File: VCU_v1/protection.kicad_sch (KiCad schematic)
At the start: 3 parts, among them Q1 PMOS

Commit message: left to do before layout: wire DRS/Debug LEDs to connector, add BRUHbus ports
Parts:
- added D7: SMBJ30CA, symbol Device:D_TVS
- D2: value 12Vz -> 27Vz; LCSC P/N C669032 -> C712317; Mouser P/N 833-SMAF4742A-TP -> 833-SMAF4750A-TP; P/N SMAF4742A-TP -> SMAF4750A-TP
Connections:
- net GND: now also D7.1 (A1)
- net VBAT_FILT: now also D7.2 (A2)
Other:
- note added: "Reverse Polarity Protection + TVS"
- note removed: "Reverse Polarity Protection"
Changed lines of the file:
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@@
 	(rectangle
 		(start 68.58 41.91)
-		(end 129.54 87.63)
+		(end 171.45 87.63)
 		(stroke
 			(width 0)
@@
 		)
 	)
-	(text "Reverse Polarity Protection\n"
+	(text "Reverse Polarity Protection + TVS\n\n"
 		(exclude_from_sim no)
 		(at 97.536 38.862 0)
@@
 	)
 	(junction
+		(at 127 57.15)
+		(diameter 0)
+		(color 0 0 0 0)
+	)
+	(junction
 		(at 106.68 57.15)
 		(diameter 0)
@@
 	(wire
 		(pts
+			(xy 127 57.15) (xy 152.4 57.15)
+		)
+		(stroke
+			(width 0)
+			(type default)
+		)
+	)
+	(wire
+		(pts
 			(xy 78.74 57.15) (xy 90.17 57.15)
 		)
@@
 	(wire
 		(pts
-			(xy 106.68 57.15) (xy 114.3 57.15)
+			(xy 106.68 57.15) (xy 127 57.15)
 		)
 		(stroke
@@
 	(wire
 		(pts
+			(xy 127 62.23) (xy 127 57.15)
+		)
+		(stroke
+			(width 0)
+			(type default)
+		)
+	)
+	(wire
+		(pts
 			(xy 95.25 73.66) (xy 95.25 76.2)
+		)
+		(stroke
+			(width 0)
+			(type default)
+		)
+	)
+	(wire
+		(pts
+			(xy 127 69.85) (xy 127 76.2)
 		)
 		(stroke
@@
 	(hierarchical_label "VBAT_FILT"
 		(shape input)
-		(at 114.3 57.15 0)
+		(at 152.4 57.15 0)
 		(effects
 			(font
@@
 			)
 		)
-		(property "Value" "12Vz"
+		(property "Value" "27Vz"
 			(at 109.22 62.2299 90)
 			(effects
@@
 			)
 		)
-		(property "P/N" "SMAF4742A-TP "
+		(property "P/N" "SMAF4750A-TP "
 			(at 106.68 60.96 90)
 			(effects
@@
 			)
 		)
-		(property "Mouser P/N" "833-SMAF4742A-TP"
+		(property "Mouser P/N" "833-SMAF4750A-TP "
 			(at 106.68 60.96 90)
 			(effects
@@
 			)
 		)
-		(property "LCSC P/N" "C669032"
+		(property "LCSC P/N" "C712317"
 			(at 106.68 60.96 90)
 			(effects
@@
 				(path "/4ee6c2ad-9a1b-4276-b3cf-1cc8dc52967e/9e4b5f8d-93dc-46d5-aa92-d0e0d2e07b3d/b7d8a0a7-c635-4617-919c-9464d63ae6b1"
 					(reference "D2")
+					(unit 1)
+				)
+			)
+		)
+	)
+	(symbol
+		(lib_id "power:GND")
+		(at 127 76.2 0)
+		(unit 1)
+		(exclude_from_sim no)
+		(in_bom yes)
+		(on_board yes)
+		(dnp no)
+		(fields_autoplaced yes)
+		(property "Reference" "#PWR0102"
+			(at 127 82.55 0)
+			(effects
+				(font
+					(size 1.27 1.27)
+				)
+				(hide yes)
+			)
+		)
+		(property "Value" "GND"
+			(at 127 81.28 0)
+			(effects
+				(font
+					(size 1.27 1.27)
+				)
+			)
+		)
+		(property "Footprint" ""
+			(at 127 76.2 0)
+			(effects
+				(font
+					(size 1.27 1.27)
+				)
+				(hide yes)
+			)
+		)
+		(property "Datasheet" ""
+			(at 127 76.2 0)
+			(effects
+				(font
+					(size 1.27 1.27)
+				)
+				(hide yes)
+			)
+		)
+		(property "Description" "Power symbol creates a global label with name \"GND\" , ground"
+			(at 127 76.2 0)
+			(effects
+				(font
+					(size 1.27 1.27)
+				)
+				(hide yes)
+			)
+		)
+		(pin "1"
+		)
+		(instances
+			(project "VCU_v1"
+				(path "/4ee6c2ad-9a1b-4276-b3cf-1cc8dc52967e/9e4b5f8d-93dc-46d5-aa92-d0e0d2e07b3d/b7d8a0a7-c635-4617-919c-9464d63ae6b1"
+					(reference "#PWR0102")
 					(unit 1)
 				)
@@
 					(unit 1)
 				)
+			)
+		)
+	)
+	(symbol
+		(lib_id "Device:D_TVS")
+		(at 127 66.04 90)
+		(unit 1)
+		(exclude_from_sim no)
+		(in_bom yes)
+		(on_board yes)
+		(dnp no)
+		(fields_autoplaced yes)
+		(property "Reference" "D7"
+			(at 129.54 64.7699 90)
+			(effects
+				(font
+					(size 1.27 1.27)
+				)
+				(justify right)
+			)
+		)
+		(property "Value" "SMBJ30CA"
+			(at 129.54 67.3099 90)
+			(effects
+				(font
+					(size 1.27 1.27)
+				)
+				(justify right)
+			)
+		)
+		(property "Footprint" ""
+			(at 127 66.04 0)
+			(effects
+				(font
+					(size 1.27 1.27)
+				)
+				(hide yes)
+			)
+		)
+		(property "Datasheet" "https://www.littelfuse.com/page-not-found?url=/assetdocs/tvs-diodes-smbj-series-datasheet?assetguid=09A6AE9A-73CB-4AC4-ACAC-E6DAB92AB953"
+			(at 127 66.04 0)
+			(effects
+				(font
+					(size 1.27 1.27)
+				)
+				(hide yes)
+			)
+		)
+		(property "Description" "Bidirectional transient-voltage-suppression diode"
+			(at 127 66.04 0)
+			(effects
+				(font
+					(size 1.27 1.27)
+				)
+				(hide yes)
+			)
+		)
+		(property "P/N" "SMBJ30CA"
+			(at 127 66.04 90)
+			(effects
+				(font
+					(size 1.27 1.27)
+				)
+				(hide yes)
+			)
+		)
+		(property "Mouser P/N" "576-SMBJ30CA "
+			(at 127 66.04 90)
+			(effects
+				(font
+					(size 1.27 1.27)
+				)
+				(hide yes)
+			)
+		)
+		(property "LCSC P/N" "C8837"
+			(at 127 66.04 90)
+			(effects
+				(font
+					(size 1.27 1.27)
+				)
+				(hide yes)
+			)
+		)
+		(pin "1"
+		)
+		(pin "2"
+		)
+		(instances
+			(project ""
+				(path "/4ee6c2ad-9a1b-4276-b3cf-1cc8dc52967e/9e4b5f8d-93dc-46d5-aa92-d0e0d2e07b3d/b7d8a0a7-c635-4617-919c-9464d63ae6b1"
+					(reference "D7")
+					(unit 1)
+				)

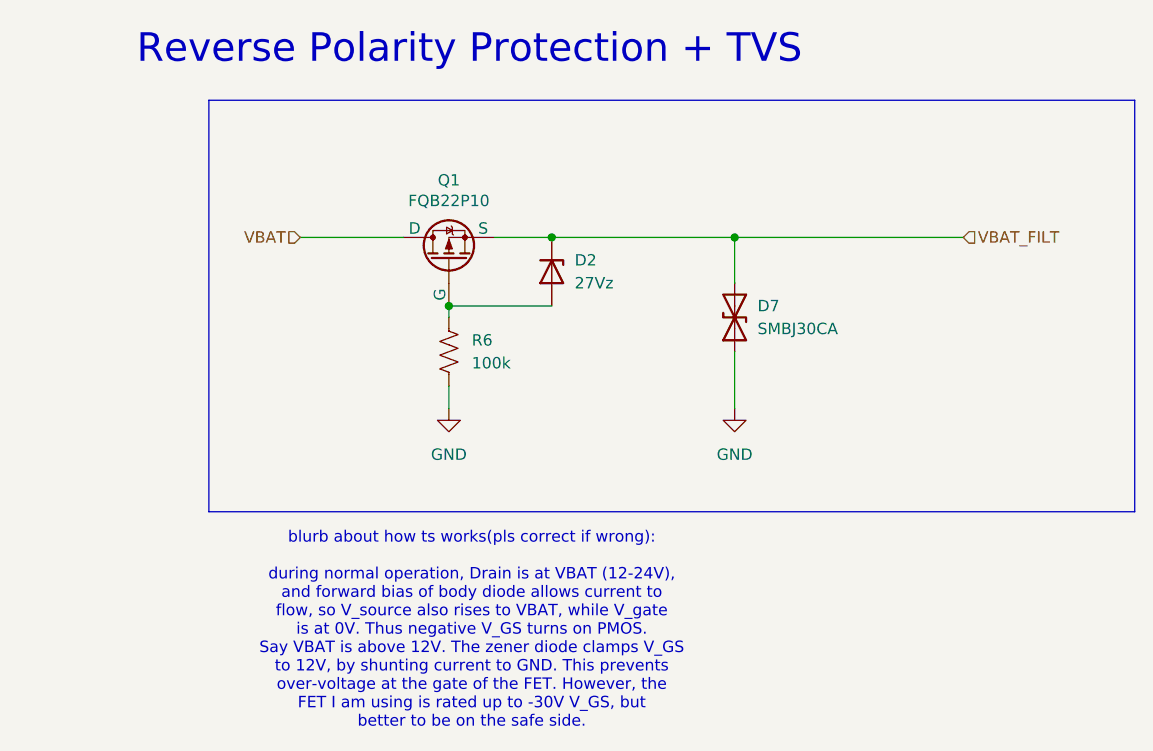
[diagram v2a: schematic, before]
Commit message: v1 schematic (actually) complete, let the layout commence
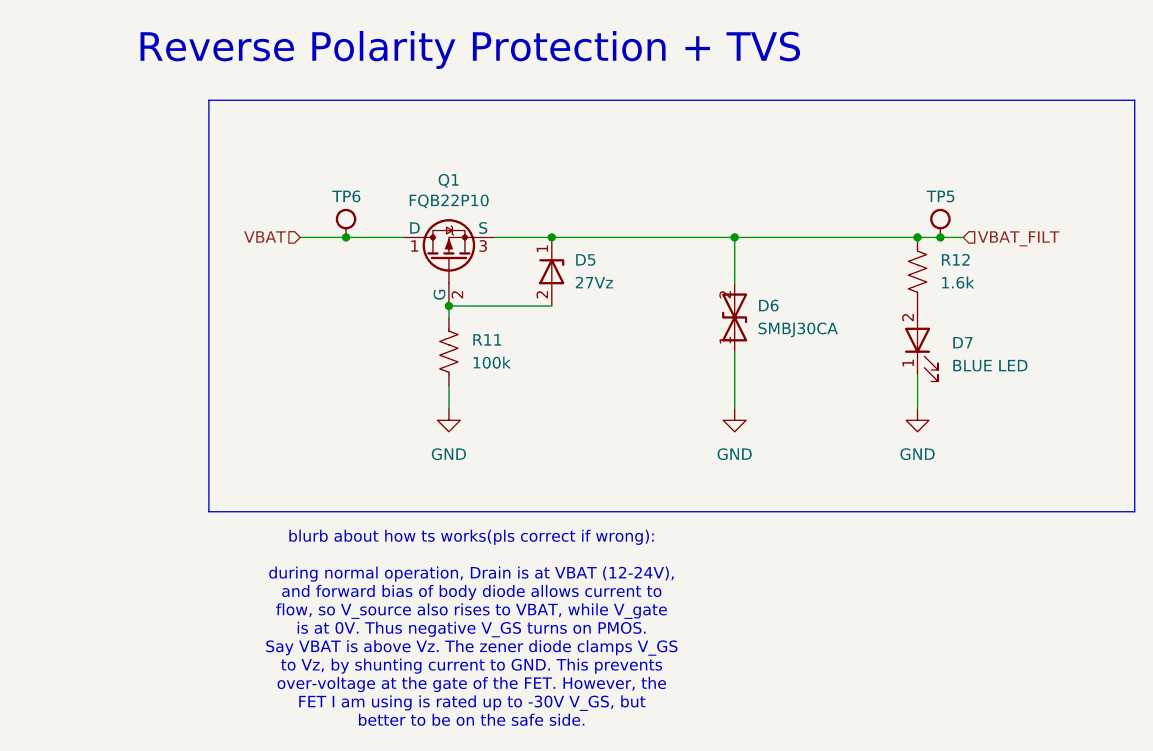
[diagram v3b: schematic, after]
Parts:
- added D7: BLUE LED, LED_SMD:LED_0201_0603Metric_Pad0.64x0.40mm_HandSolder, symbol Device:LED
- added R12: 1.6k, Resistor_SMD:R_0603_1608Metric_Pad0.98x0.95mm_HandSolder, symbol BFR Resistors:RMCF0603FT1K60
- added TP5, TP6: RH-5015, TestPoint:TestPoint_Keystone_5015_Micro_Mini, symbol .Test-Point:RH-5015
- D5: renamed from D2; footprint (none) -> Diode_SMD:D_SMA
- D6: renamed from D7; footprint (none) -> Diode_SMD:D_SMB
- Q1: footprint (none) -> FQB22P10:Untitled
- renumbered R6 to R11
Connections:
- net GND: now also D7.1 (K)
- net VBAT: now also TP6.1
- net VBAT_FILT: now also R12.2, TP5.1
- new net: D7.2 (A), R12.1
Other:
- note added: "blurb about how ts works(pls correct if wrong): during normal operation, Drain is at VBAT (12-24V), and forward bias of body diode allows current to flow, so V_source also rises to VBAT, while V_gate is at 0V. Thus negative V_GS turns on PMOS. Say VBAT is above Vz. The zener diode clamps V_GS to Vz, by shunting current to GND. This prevents over-voltage at the gate of the FET. However, the FET I 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"
- note removed: "blurb about how ts works(pls correct if wrong): during normal operation, Drain is at VBAT (12-24V), and forward bias of body diode allows current to flow, so V_source also rises to VBAT, while V_gate is at 0V. Thus negative V_GS turns on PMOS. Say VBAT is above 12V. The zener diode clamps V_GS to 12V, by shunting current to GND. This prevents over-voltage at the gate of the FET. However, the FET 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"

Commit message: vcu placements complete
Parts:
- D7: footprint LED_SMD:LED_0201_0603Metric_Pad0.64x0.40mm_HandSolder -> LED_SMD:LED_0603_1608Metric_Pad1.05x0.95mm_HandSolder
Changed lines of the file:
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@@
 			)
 		)
-		(property "Footprint" "LED_SMD:LED_0201_0603Metric_Pad0.64x0.40mm_HandSolder"
+		(property "Footprint" "LED_SMD:LED_0603_1608Metric_Pad1.05x0.95mm_HandSolder"
 			(at 147.32 68.58 0)
 			(effects

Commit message: almost done i promise
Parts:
- removed R12: 1.6k, Resistor_SMD:R_0603_1608Metric_Pad0.98x0.95mm_HandSolder, symbol BFR Resistors:RMCF0603FT1K60
- added R3: 2.4k, Resistor_SMD:R_0603_1608Metric_Pad0.98x0.95mm_HandSolder, symbol BFR Resistors:RMCF0603FT2K40
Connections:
- net VBAT_FILT: now also R3.2
- net at D7.2 (A): now also R3.1
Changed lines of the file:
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@@
+	)
+	(junction
+		(at 147.32 57.15)
+		(diameter 0)
+		(color 0 0 0 0)
 	)
 	(junction
@@
 	)
 	(junction
-		(at 147.32 57.15)
-		(diameter 0)
-		(color 0 0 0 0)
-	)
-	(junction
 		(at 83.82 57.15)
 		(diameter 0)
@@
 	(wire
 		(pts
-			(xy 147.32 57.15) (xy 149.86 57.15)
+			(xy 83.82 57.15) (xy 90.17 57.15)
 		)
 		(stroke
@@
 	(wire
 		(pts
-			(xy 83.82 57.15) (xy 90.17 57.15)
+			(xy 78.74 57.15) (xy 83.82 57.15)
 		)
 		(stroke
@@
 	(wire
 		(pts
-			(xy 78.74 57.15) (xy 83.82 57.15)
+			(xy 106.68 57.15) (xy 127 57.15)
 		)
 		(stroke
@@
 	(wire
 		(pts
-			(xy 106.68 57.15) (xy 127 57.15)
+			(xy 95.25 64.77) (xy 106.68 64.77)
 		)
 		(stroke
@@
 	(wire
 		(pts
-			(xy 95.25 64.77) (xy 106.68 64.77)
+			(xy 100.33 57.15) (xy 106.68 57.15)
 		)
 		(stroke
@@
 	(wire
 		(pts
-			(xy 100.33 57.15) (xy 106.68 57.15)
+			(xy 147.32 57.15) (xy 149.86 57.15)
 		)
 		(stroke
@@
 				(path "/4ee6c2ad-9a1b-4276-b3cf-1cc8dc52967e/9e4b5f8d-93dc-46d5-aa92-d0e0d2e07b3d/b7d8a0a7-c635-4617-919c-9464d63ae6b1"
 					(reference "Q1")
-					(unit 1)
-				)
-			)
-		)
-	)
-	(symbol
-		(lib_id "BFR Resistors:RMCF0603FT1K60")
-		(at 147.32 60.96 90)
-		(unit 1)
-		(exclude_from_sim no)
-		(in_bom yes)
-		(on_board yes)
-		(dnp no)
-		(fields_autoplaced yes)
-		(property "Reference" "R12"
-			(at 149.86 59.6899 90)
-			(effects
-				(font
-					(size 1.27 1.27)
-				)
-				(justify right)
-			)
-		)
-		(property "Value" "1.6k"
-			(at 149.86 62.2299 90)
-			(effects
-				(font
-					(size 1.27 1.27)
-				)
-				(justify right)
-			)
-		)
-		(property "Footprint" "Resistor_SMD:R_0603_1608Metric_Pad0.98x0.95mm_HandSolder"
-			(at 149.86 60.96 0)
-			(effects
-				(font
-					(size 1.27 1.27)
-				)
-				(hide yes)
-			)
-		)
-		(property "Datasheet" "https://www.seielect.com/catalog/sei-rmcf_rmcp.pdf"
-			(at 151.13 60.96 0)
-			(effects
-				(font
-					(size 1.27 1.27)
-				)
-				(hide yes)
-			)
-		)
-		(property "Description" "1.6kΩ 0603 Resistor"
-			(at 147.32 60.96 0)
-			(effects
-				(font
-					(size 1.27 1.27)
-				)
-				(hide yes)
-			)
-		)
-		(property "Sim.Device" "SUBCKT"
-			(at 152.4 60.96 0)
-			(effects
-				(font
-					(size 1.27 1.27)
-				)
-				(hide yes)
-			)
-		)
-		(property "Sim.Pins" "1=P1 2=P2"
-			(at 153.67 60.96 0)
-			(effects
-				(font
-					(size 1.27 1.27)
-				)
-				(hide yes)
-			)
-		)
-		(property "Sim.Library" "${BFRUH_DIR}/Electronics/spice_models/bfr_resistors/RMCF0603FT1K60.lib"
-			(at 154.94 60.96 0)
-			(effects
-				(font
-					(size 1.27 1.27)
-				)
-				(hide yes)
-			)
-		)
-		(property "Sim.Name" "RMCF0603FT1K60"
-			(at 156.21 60.96 0)
-			(effects
-				(font
-					(size 1.27 1.27)
-				)
-				(hide yes)
-			)
-		)
-		(property "Pretty Name" "1.6kΩ 0603 Resistor"
-			(at 157.48 60.96 0)
-			(effects
-				(font
-					(size 1.27 1.27)
-				)
-				(hide yes)
-			)
-		)
-		(property "Qty/Unit" ""
-			(at 158.75 60.96 0)
-			(effects
-				(font
-					(size 1.27 1.27)
-				)
-				(hide yes)
-			)
-		)
-		(property "Cost/Unit" ""
-			(at 160.02 60.96 0)
-			(effects
-				(font
-					(size 1.27 1.27)
-				)
-				(hide yes)
-			)
-		)
-		(property "Order From" "Mouser"
-			(at 161.29 60.96 0)
-			(effects
-				(font
-					(size 1.27 1.27)
-				)
-				(hide yes)
-			)
-		)
-		(property "Digikey P/N" "RMCF0603FT1K60CT-ND"
-			(at 162.56 60.96 0)
-			(effects
-				(font
-					(size 1.27 1.27)
-				)
-				(hide yes)
-			)
-		)
-		(property "Mouser P/N" "708-RMCF0603FT1K60"
-			(at 162.56 60.96 0)
-			(effects
-				(font
-					(size 1.27 1.27)
-				)
-				(hide yes)
-			)
-		)
-		(property "LCSC P/N" "C22847"
-			(at 162.56 60.96 0)
-			(effects
-				(font
-					(size 1.27 1.27)
-				)
-				(hide yes)
-			)
-		)
-		(property "JLCPCB Basic Part" "No"
-			(at 162.56 60.96 0)
-			(effects
-				(font
-					(size 1.27 1.27)
-				)
-				(hide yes)
-			)
-		)
-		(property "Created by" "resistor_generator.py script using e24_resistor_bible_spec.txt"
-			(at 162.56 60.96 0)
-			(effects
-				(font
-					(size 1.27 1.27)
-				)
-				(hide yes)
-			)
-		)
-		(pin "2"
-		)
-		(pin "1"
-		)
-		(instances
-			(project "VCU_v1"
-				(path "/4ee6c2ad-9a1b-4276-b3cf-1cc8dc52967e/9e4b5f8d-93dc-46d5-aa92-d0e0d2e07b3d/b7d8a0a7-c635-4617-919c-9464d63ae6b1"
-					(reference "R12")
 					(unit 1)
 				)
@@
 					(unit 1)
 				)
+			)
+		)
+	)
+	(symbol
+		(lib_id "BFR Resistors:RMCF0603FT2K40")
+		(at 147.32 60.96 90)
+		(unit 1)
+		(exclude_from_sim no)
+		(in_bom yes)
+		(on_board yes)
+		(dnp no)
+		(fields_autoplaced yes)
+		(property "Reference" "R3"
+			(at 149.86 59.6899 90)
+			(effects
+				(font
+					(size 1.27 1.27)
+				)
+				(justify right)
+			)
+		)
+		(property "Value" "2.4k"
+			(at 149.86 62.2299 90)
+			(effects
+				(font
+					(size 1.27 1.27)
+				)
+				(justify right)
+			)
+		)
+		(property "Footprint" "Resistor_SMD:R_0603_1608Metric_Pad0.98x0.95mm_HandSolder"
+			(at 149.86 60.96 0)
+			(effects
+				(font
+					(size 1.27 1.27)
+				)
+				(hide yes)
+			)
+		)
+		(property "Datasheet" "https://www.seielect.com/catalog/sei-rmcf_rmcp.pdf"
+			(at 151.13 60.96 0)
+			(effects
+				(font
+					(size 1.27 1.27)
+				)
+				(hide yes)
+			)
+		)
+		(property "Description" "2.4kΩ 0603 JLCPCB Basic Resistor"
+			(at 147.32 60.96 0)
+			(effects
+				(font
+					(size 1.27 1.27)
+				)
+				(hide yes)
+			)
+		)
+		(property "Sim.Device" "SUBCKT"
+			(at 152.4 60.96 0)
+			(effects
+				(font
+					(size 1.27 1.27)
+				)
+				(hide yes)
+			)
+		)
+		(property "Sim.Pins" "1=P1 2=P2"
+			(at 153.67 60.96 0)
+			(effects
+				(font
+					(size 1.27 1.27)
+				)
+				(hide yes)
+			)
+		)
+		(property "Sim.Library" "${BFRUH_DIR}/Electronics/spice_models/bfr_resistors/RMCF0603FT2K40.lib"
+			(at 154.94 60.96 0)
+			(effects
+				(font
+					(size 1.27 1.27)
+				)
+				(hide yes)
+			)
+		)
+		(property "Sim.Name" "RMCF0603FT2K40"
+			(at 156.21 60.96 0)
+			(effects
+				(font
+					(size 1.27 1.27)
+				)
+				(hide yes)
+			)
+		)
+		(property "Pretty Name" "2.4kΩ 0603 Resistor"
+			(at 157.48 60.96 0)
+			(effects
+				(font
+					(size 1.27 1.27)
+				)
+				(hide yes)
+			)
+		)
+		(property "Qty/Unit" ""
+			(at 158.75 60.96 0)
+			(effects
+				(font
+					(size 1.27 1.27)
+				)
+				(hide yes)
+			)
+		)
+		(property "Cost/Unit" ""
+			(at 160.02 60.96 0)
+			(effects
+				(font
+					(size 1.27 1.27)
+				)
+				(hide yes)
+			)
+		)
+		(property "Order From" "LCSC"
+			(at 161.29 60.96 0)
+			(effects
+				(font
+					(size 1.27 1.27)
+				)
+				(hide yes)
+			)
+		)
+		(property "Digikey P/N" "RMCF0603FT2K40CT-ND"
+			(at 162.56 60.96 0)
+			(effects
+				(font
+					(size 1.27 1.27)
+				)
+				(hide yes)
+			)
+		)
+		(property "Mouser P/N" "708-RMCF0603FT2K40"
+			(at 162.56 60.96 0)
+			(effects
+				(font
+					(size 1.27 1.27)
+				)
+				(hide yes)
+			)
+		)
+		(property "LCSC P/N" "C22940"
+			(at 162.56 60.96 0)
+			(effects
+				(font
+					(size 1.27 1.27)
+				)
+				(hide yes)
+			)
+		)
+		(property "JLCPCB Basic Part" "Yes"
+			(at 162.56 60.96 0)
+			(effects
+				(font
+					(size 1.27 1.27)
+				)
+				(hide yes)
+			)
+		)
+		(property "Created by" "resistor_generator.py script using e24_resistor_bible_spec.txt"
+			(at 162.56 60.96 0)
+			(effects
+				(font
+					(size 1.27 1.27)
+				)
+				(hide yes)
+			)
+		)
+		(pin "1"
+		)
+		(pin "2"
+		)
+		(instances
+			(project ""
+				(path "/4ee6c2ad-9a1b-4276-b3cf-1cc8dc52967e/9e4b5f8d-93dc-46d5-aa92-d0e0d2e07b3d/b7d8a0a7-c635-4617-919c-9464d63ae6b1"
+					(reference "R3")
+					(unit 1)
+				)
